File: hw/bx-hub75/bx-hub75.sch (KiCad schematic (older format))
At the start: 11 parts, among them J1 DB9_Male, U1 74HCT541, U2 74HCT541, U3 LD1117S33TR_SOT223, U4 25LCxxx, U5 SN65HVD77D

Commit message: hw/bx-hub75: oshw logo, text, extension header
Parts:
- added EXT1: EXT_HEADER, Random:EXT_HEADER, symbol Random:EXT_HEADER
- renumbered U4 to EEPROM1, U5 to RS485
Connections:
- net +3V3: now also EXT1.2 (3V3)
- net GND: now also EXT1.1 (GND)
- net MISO: now also EXT1.5 (MISO)
- net MOSI: now also EXT1.4 (MOSI)
- net SCK: now also EXT1.3 (SCK)
- net SC_EXT: now reaches FPGA1.21 (IO_20)
- net SC_EXT: now also EXT1.6 (SC)
- net EXT_IO1: now reaches FPGA1.22 (IO_21)
- net EXT_IO1: now also EXT1.7 (IO_1)
- net EXT_IO2: now reaches FPGA1.23 (IO_22)
- net EXT_IO2: now also EXT1.8 (IO_2)
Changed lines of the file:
@@
 G1
 $Comp
-L Random:SN65HVD77D U5
+L Random:SN65HVD77D RS485
 U 1 1 5BECF5D6
 P 7600 5150
-F 0 "U5" H 7600 5525 50  0000 C CNN
+F 0 "RS485" H 7600 5525 50  0000 C CNN
 F 1 "SN65HVD77D" H 7600 5434 50  0000 C CNN
 F 2 "Package_SO:SOIC-8_3.9x4.9mm_P1.27mm" H 7600 4900 50  0001 C CNN
@@
 	3400 5000 3150 5000
 $Comp
-L Memory_EEPROM:25LCxxx U4
+L Memory_EEPROM:25LCxxx EEPROM1
 U 1 1 5BF300CE
 P 5100 5100
-F 0 "U4" H 5100 5578 50  0000 C CNN
+F 0 "EEPROM1" H 5100 5578 50  0000 C CNN
 F 1 "25LCxxx" H 5100 5487 50  0000 C CNN
 F 2 "Package_SO:SOIC-8_3.9x4.9mm_P1.27mm" H 5100 5100 50  0001 C CNN
@@
 	8100 2350 8100 2250
 Connection ~ 8100 2250
+$Comp
+L Random:EXT_HEADER EXT1
+U 1 1 5BFBA84B
+P 9350 2450
+F 0 "EXT1" H 9528 2401 50  0000 L CNN
+F 1 "EXT_HEADER" H 9528 2310 50  0000 L CNN
+F 2 "Random:EXT_HEADER" H 9350 2800 50  0001 C CNN
+F 3 "" H 9350 2800 50  0001 C CNN
+	1    9350 2450
+	1    0    0    -1
+$EndComp
+$Comp
+L power:GND #PWR0116
+U 1 1 5BFBAE0E
+P 8800 2050
+F 0 "#PWR0116" H 8800 1800 50  0001 C CNN
+F 1 "GND" H 8805 1877 50  0000 C CNN
+F 2 "" H 8800 2050 50  0001 C CNN
+F 3 "" H 8800 2050 50  0001 C CNN
+	1    8800 2050
+	1    0    0    -1
+$EndComp
+$Comp
+L power:+3V3 #PWR0117
+U 1 1 5BFBAE5B
+P 8600 2300
+F 0 "#PWR0117" H 8600 2150 50  0001 C CNN
+F 1 "+3V3" H 8615 2473 50  0000 C CNN
+F 2 "" H 8600 2300 50  0001 C CNN
+F 3 "" H 8600 2300 50  0001 C CNN
+	1    8600 2300
+	1    0    0    -1
+$EndComp
+Wire Wire Line
+	8600 2300 9050 2300
+Wire Wire Line
+	9050 2200 9050 2050
+Wire Wire Line
+	9050 2050 8800 2050
+Text Label 9050 2400 2    50   ~ 0
+SCK
+Text Label 9050 2500 2    50   ~ 0
+MOSI
+Text Label 9050 2600 2    50   ~ 0
+MISO
+Text Label 9050 2700 2    50   ~ 0
+SC_EXT
+Text Label 9050 2800 2    50   ~ 0
+EXT_IO1
+Text Label 9050 2900 2    50   ~ 0
+EXT_IO2
+Text Label 2350 2750 2    50   ~ 0
+SC_EXT
+Text Label 2350 2850 2    50   ~ 0
+EXT_IO1
+Text Label 2350 2950 2    50   ~ 0
+EXT_IO2
 $EndSCHEMATC

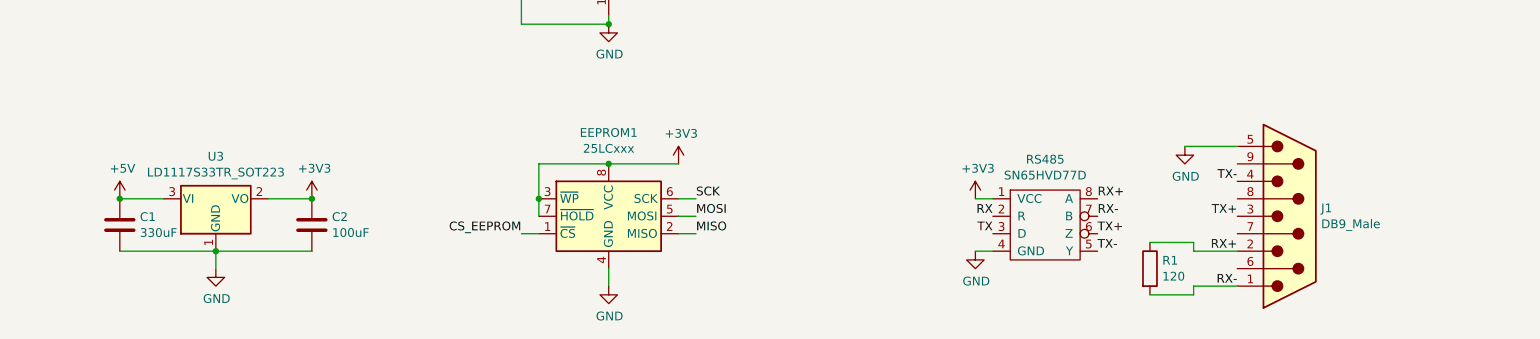
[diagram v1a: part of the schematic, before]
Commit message: hw/bx-hub75: add barrel jack
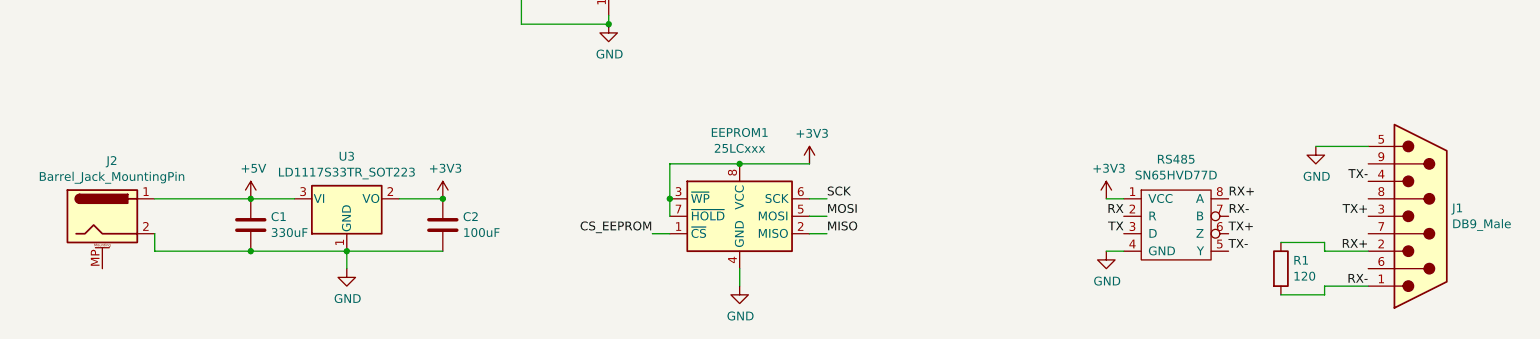
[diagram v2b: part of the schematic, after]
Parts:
- added J2: Barrel_Jack_MountingPin, Connector_BarrelJack:BarrelJack_CUI_PJ-063AH_Horizontal, symbol Connector:Barrel_Jack_MountingPin
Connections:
- net +5V: now also J2.1
- net GND: now also J2.2
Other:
- moved on the sheet: C1, C2, EEPROM1, J1, R1, RS485, U3

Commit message: hw/bx-hub75: allow bom generation with kibom
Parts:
- CHAIN1, EXT1, FPGA1: fit_field (none) -> DNF
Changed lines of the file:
@@
 F 2 "TinyFPGA:TinyFPGA_BX" H 3000 3550 50  0001 C CNN
 F 3 "" H 3000 3550 50  0001 C CNN
+F 4 "DNF" H 2850 2850 50  0001 C CNN "fit_field"
 	1    2850 2850
 	-1   0    0    1
@@
 F 2 "Random:HUB75_HEADER" H 6350 2550 50  0001 C CNN
 F 3 "" H 6350 2550 50  0001 C CNN
+F 4 "DNF" H 6350 3000 50  0001 C CNN "fit_field"
 	1    6350 3000
 	1    0    0    -1
@@
 F 2 "Random:EXT_HEADER" H 9350 2800 50  0001 C CNN
 F 3 "" H 9350 2800 50  0001 C CNN
+F 4 "DNF" H 9350 2450 50  0001 C CNN "fit_field"
 	1    9350 2450
 	1    0    0    -1

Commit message: hw/bx-hub75: V0.2 PCB/SCH.
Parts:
- added JP1: Jumper_NO_Small, Connector_PinHeader_2.54mm:PinHeader_1x02_P2.54mm_Vertical, symbol Device:Jumper_NO_Small
- added R2: 120, Resistor_SMD:R_1210_3225Metric_Pad1.42x2.65mm_HandSolder, symbol Device:R
- EXT1: footprint Random:EXT_HEADER -> Connector_PinHeader_2.54mm:PinHeader_1x08_P2.54mm_Vertical
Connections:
- net +5V: now also JP1.2
- net TX+: now also R2.2
- net TX-: now also R2.1
- net at J1.6: now also JP1.1
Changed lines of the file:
@@
 F 1 "SN65HVD77D" H 8350 5434 50  0000 C CNN
 F 2 "Package_SO:SOIC-8_3.9x4.9mm_P1.27mm" H 8350 4900 50  0001 C CNN
-F 3 "" H 8350 4900 50  0001 C CNN
+F 3 "http://www.ti.com/lit/ds/symlink/sn65hvd77.pdf" H 8350 4900 50  0001 C CNN
 	1    8350 5150
 	1    0    0    -1
@@
 L power:GND #PWR0109
 U 1 1 5BEDE34B
-P 9150 4700
-F 0 "#PWR0109" H 9150 4450 50  0001 C CNN
-F 1 "GND" H 9155 4527 50  0000 C CNN
-F 2 "" H 9150 4700 50  0001 C CNN
-F 3 "" H 9150 4700 50  0001 C CNN
-	1    9150 4700
-	1    0    0    -1
-$EndComp
-Wire Wire Line
-	9150 4700 9450 4700
+P 9150 4400
+F 0 "#PWR0109" H 9150 4150 50  0001 C CNN
+F 1 "GND" H 9155 4227 50  0000 C CNN
+F 2 "" H 9150 4400 50  0001 C CNN
+F 3 "" H 9150 4400 50  0001 C CNN
+	1    9150 4400
+	1    0    0    -1
+$EndComp
 $Comp
 L Device:R R1
@@
 F 0 "EXT1" H 9528 2401 50  0000 L CNN
 F 1 "EXT_HEADER" H 9528 2310 50  0000 L CNN
-F 2 "Random:EXT_HEADER" H 9350 2800 50  0001 C CNN
+F 2 "Connector_PinHeader_2.54mm:PinHeader_1x08_P2.54mm_Vertical" H 9350 2800 50  0001 C CNN
 F 3 "" H 9350 2800 50  0001 C CNN
 F 4 "DNF" H 9350 2450 50  0001 C CNN "fit_field"
@@
 	2500 5300 3050 5300
 Connection ~ 3050 5300
+$Comp
+L Device:R R2
+U 1 1 5C0B21F0
+P 8950 5000
+F 0 "R2" H 9020 5046 50  0000 L CNN
+F 1 "120" H 9020 4955 50  0000 L CNN
+F 2 "Resistor_SMD:R_1210_3225Metric_Pad1.42x2.65mm_HandSolder" V 8880 5000 50  0001 C CNN
+F 3 "~" H 8950 5000 50  0001 C CNN
+F 4 "dnf" H 8950 5000 50  0001 C CNN "fit_field"
+	1    8950 5000
+	1    0    0    -1
+$EndComp
+Wire Wire Line
+	8950 5150 9200 5150
+Wire Wire Line
+	9200 5150 9200 5100
+Wire Wire Line
+	9200 5100 9450 5100
+Wire Wire Line
+	9450 4900 9200 4900
+Wire Wire Line
+	9200 4900 9200 4850
+Wire Wire Line
+	9200 4850 8950 4850
+Wire Wire Line
+	9450 4700 9450 4400
+Wire Wire Line
+	9450 4400 9150 4400
+$Comp
+L power:+5V #PWR0118
+U 1 1 5C0C1F94
+P 10000 5950
+F 0 "#PWR0118" H 10000 5800 50  0001 C CNN
+F 1 "+5V" H 10015 6123 50  0000 C CNN
+F 2 "" H 10000 5950 50  0001 C CNN
+F 3 "" H 10000 5950 50  0001 C CNN
+	1    10000 5950
+	1    0    0    -1
+$EndComp
+$Comp
+L Device:Jumper_NO_Small JP1
+U 1 1 5C0C5F7A
+P 9600 5950
+F 0 "JP1" H 9600 6135 50  0000 C CNN
+F 1 "Jumper_NO_Small" H 9600 6044 50  0000 C CNN
+F 2 "Connector_PinHeader_2.54mm:PinHeader_1x02_P2.54mm_Vertical" H 9600 5950 50  0001 C CNN
+F 3 "~" H 9600 5950 50  0001 C CNN
+	1    9600 5950
+	1    0    0    -1
+$EndComp
+Wire Wire Line
+	9450 5400 9250 5400
+Wire Wire Line
+	9250 5400 9250 5950
+Wire Wire Line
+	9500 5950 9250 5950
+Wire Wire Line
+	10000 5950 9700 5950
 $EndSCHEMATC

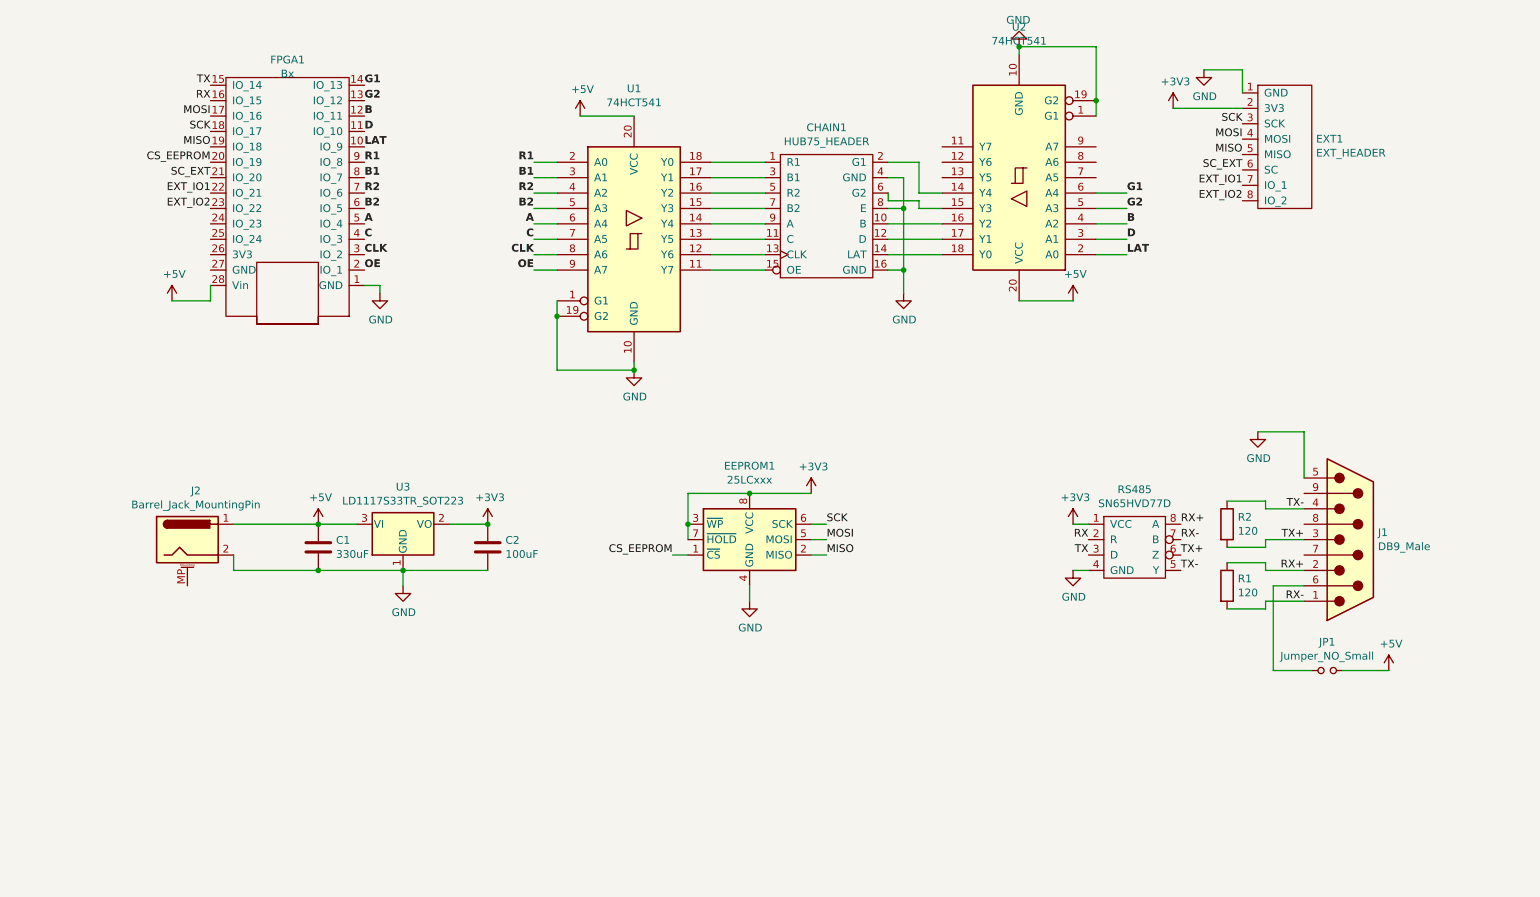
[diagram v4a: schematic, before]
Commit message: hw/bx-hub75: v0.3, E Line support.
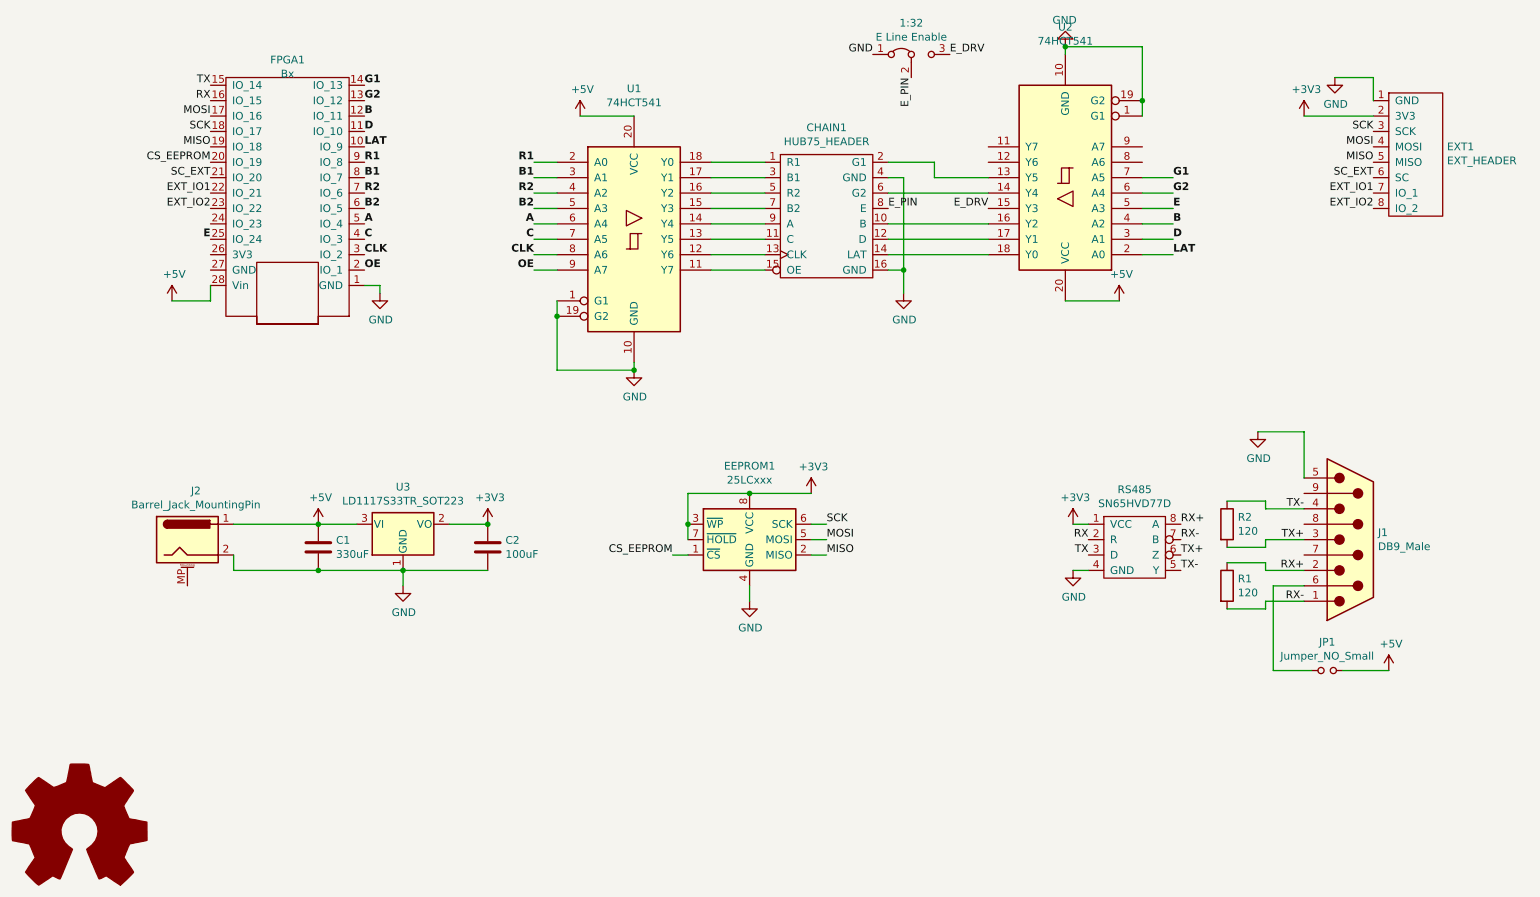
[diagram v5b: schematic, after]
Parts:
- added 1:32: E Line Enable, Connector_PinHeader_2.54mm:PinHeader_1x03_P2.54mm_Vertical, symbol Jumper:Jumper_3_Bridged12
- added OSHW1: Logo_Open_Hardware_Large, Symbol:OSHW-Logo2_9.8x8mm_SilkScreen, symbol Graphic:Logo_Open_Hardware_Large
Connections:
- net G1: now also U2.7 (A5); no longer U2.6 (A4)
- net G2: now also U2.6 (A4); no longer U2.5 (A3)
- net GND: now also 1:32.1 (A); no longer CHAIN1.8 (E)
- net E: now reaches FPGA1.25 (IO_24)
- net E: now also U2.5 (A3)
- net at CHAIN1.2 (G1): now also U2.13 (Y5); no longer U2.14 (Y4)
- net at CHAIN1.6 (G2): now also U2.14 (Y4); no longer U2.15 (Y3)
- new net E_DRV: 1:32.3 (B), U2.15 (Y3)
- new net E_PIN: 1:32.2 (C), CHAIN1.8 (E)
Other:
- moved on the sheet: EXT1, U2
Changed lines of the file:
@@
 L power:GND #PWR0103
 U 1 1 5BECC23F
-P 7600 1900
-F 0 "#PWR0103" H 7600 1650 50  0001 C CNN
-F 1 "GND" H 7605 1727 50  0000 C CNN
-F 2 "" H 7600 1900 50  0001 C CNN
-F 3 "" H 7600 1900 50  0001 C CNN
-	1    7600 1900
+P 7900 1900
+F 0 "#PWR0103" H 7900 1650 50  0001 C CNN
+F 1 "GND" H 7905 1727 50  0000 C CNN
+F 2 "" H 7900 1900 50  0001 C CNN
+F 3 "" H 7900 1900 50  0001 C CNN
+	1    7900 1900
 	-1   0    0    1
 $EndComp
 Wire Wire Line
-	7600 1950 7600 1900
+	7900 1950 7900 1900
 $Comp
 L power:GND #PWR0104
@@
 L power:+5V #PWR0107
 U 1 1 5BEDB676
-P 7950 3550
-F 0 "#PWR0107" H 7950 3400 50  0001 C CNN
-F 1 "+5V" H 7965 3723 50  0000 C CNN
-F 2 "" H 7950 3550 50  0001 C CNN
-F 3 "" H 7950 3550 50  0001 C CNN
-	1    7950 3550
-	1    0    0    -1
-$EndComp
-Wire Wire Line
-	7950 3550 7600 3550
+P 8250 3550
+F 0 "#PWR0107" H 8250 3400 50  0001 C CNN
+F 1 "+5V" H 8265 3723 50  0000 C CNN
+F 2 "" H 8250 3550 50  0001 C CNN
+F 3 "" H 8250 3550 50  0001 C CNN
+	1    8250 3550
+	1    0    0    -1
+$EndComp
+Wire Wire Line
+	8250 3550 7900 3550
 Wire Wire Line
 	5100 2350 4750 2350
 Wire Wire Line
-	8100 2250 8100 1900
-Wire Wire Line
-	8100 1900 7600 1900
-Connection ~ 7600 1900
+	8400 2250 8400 1900
+Wire Wire Line
+	8400 1900 7900 1900
+Connection ~ 7900 1900
 Text Label 4450 2650 2    50   ~ 10
 R1
@@
 	4600 3350 4450 3350
 Wire Wire Line
-	6850 3350 6850 2950
-Wire Wire Line
 	6850 2750 6750 2750
-Wire Wire Line
-	6750 2950 6850 2950
-Connection ~ 6850 2950
-Wire Wire Line
-	6850 2950 6850 2750
-Wire Wire Line
-	7100 3250 6750 3250
-Wire Wire Line
-	7100 3150 6750 3150
-Wire Wire Line
-	7100 3050 6750 3050
-Wire Wire Line
-	7100 2950 6950 2950
-Wire Wire Line
-	6950 2950 6950 2900
-Wire Wire Line
-	6950 2900 6750 2900
-Wire Wire Line
-	6750 2900 6750 2850
-Wire Wire Line
-	7100 2850 6950 2850
-Wire Wire Line
-	6950 2650 6750 2650
-Wire Wire Line
-	6950 2650 6950 2850
-Text Label 8300 3250 0    50   ~ 10
+Text Label 8600 3250 0    50   ~ 10
 LAT
-Text Label 8300 3150 0    50   ~ 10
+Text Label 8600 3150 0    50   ~ 10
 D
-Text Label 8300 3050 0    50   ~ 10
+Text Label 8600 3050 0    50   ~ 10
 B
-Text Label 8300 2950 0    50   ~ 10
+Text Label 8600 2850 0    50   ~ 10
 G2
-Text Label 8300 2850 0    50   ~ 10
+Text Label 8600 2750 0    50   ~ 10
 G1
 Wire Wire Line
-	8300 3250 8100 3250
-Wire Wire Line
-	8300 3150 8100 3150
-Wire Wire Line
-	8300 3050 8100 3050
-Wire Wire Line
-	8300 2950 8100 2950
-Wire Wire Line
-	8300 2850 8100 2850
+	8600 3250 8400 3250
+Wire Wire Line
+	8600 3150 8400 3150
+Wire Wire Line
+	8600 3050 8400 3050
+Wire Wire Line
+	8600 2850 8400 2850
+Wire Wire Line
+	8600 2750 8400 2750
 Wire Wire Line
 	6850 3350 6850 3500
@@
 L 74xx:74HCT541 U2
 U 1 1 5BF6300B
-P 7600 2750
-F 0 "U2" H 7600 1772 50  0000 C CNN
-F 1 "74HCT541" H 7600 1863 50  0000 C CNN
-F 2 "Package_SO:SOIC-20W_7.5x12.8mm_P1.27mm" H 7600 2750 50  0001 C CNN
-F 3 "http://www.ti.com/lit/gpn/sn74HCT541" H 7600 2750 50  0001 C CNN
-	1    7600 2750
+P 7900 2750
+F 0 "U2" H 7900 1772 50  0000 C CNN
+F 1 "74HCT541" H 7900 1863 50  0000 C CNN
+F 2 "Package_SO:SOIC-20W_7.5x12.8mm_P1.27mm" H 7900 2750 50  0001 C CNN
+F 3 "http://www.ti.com/lit/gpn/sn74HCT541" H 7900 2750 50  0001 C CNN
+	1    7900 2750
 	-1   0    0    1
 $EndComp
 Wire Wire Line
-	8100 2350 8100 2250
-Connection ~ 8100 2250
+	8400 2350 8400 2250
+Connection ~ 8400 2250
 $Comp
 L Random:EXT_HEADER EXT1
 U 1 1 5BFBA84B
-P 9350 2450
-F 0 "EXT1" H 9528 2401 50  0000 L CNN
-F 1 "EXT_HEADER" H 9528 2310 50  0000 L CNN
-F 2 "Connector_PinHeader_2.54mm:PinHeader_1x08_P2.54mm_Vertical" H 9350 2800 50  0001 C CNN
-F 3 "" H 9350 2800 50  0001 C CNN
-F 4 "DNF" H 9350 2450 50  0001 C CNN "fit_field"
-	1    9350 2450
+P 10200 2500
+F 0 "EXT1" H 10378 2451 50  0000 L CNN
+F 1 "EXT_HEADER" H 10378 2360 50  0000 L CNN
+F 2 "Connector_PinHeader_2.54mm:PinHeader_1x08_P2.54mm_Vertical" H 10200 2850 50  0001 C CNN
+F 3 "" H 10200 2850 50  0001 C CNN
+F 4 "DNF" H 10200 2500 50  0001 C CNN "fit_field"
+	1    10200 2500
 	1    0    0    -1
 $EndComp
@@
 L power:GND #PWR0116
 U 1 1 5BFBAE0E
-P 8800 2050
-F 0 "#PWR0116" H 8800 1800 50  0001 C CNN
-F 1 "GND" H 8805 1877 50  0000 C CNN
-F 2 "" H 8800 2050 50  0001 C CNN
-F 3 "" H 8800 2050 50  0001 C CNN
-	1    8800 2050
+P 9650 2100
+F 0 "#PWR0116" H 9650 1850 50  0001 C CNN
+F 1 "GND" H 9655 1927 50  0000 C CNN
+F 2 "" H 9650 2100 50  0001 C CNN
+F 3 "" H 9650 2100 50  0001 C CNN
+	1    9650 2100
 	1    0    0    -1
 $EndComp
@@
 L power:+3V3 #PWR0117
 U 1 1 5BFBAE5B
-P 8600 2300
-F 0 "#PWR0117" H 8600 2150 50  0001 C CNN
-F 1 "+3V3" H 8615 2473 50  0000 C CNN
-F 2 "" H 8600 2300 50  0001 C CNN
-F 3 "" H 8600 2300 50  0001 C CNN
-	1    8600 2300
-	1    0    0    -1
-$EndComp
-Wire Wire Line
-	8600 2300 9050 2300
-Wire Wire Line
-	9050 2200 9050 2050
-Wire Wire Line
-	9050 2050 8800 2050
-Text Label 9050 2400 2    50   ~ 0
+P 9450 2350
+F 0 "#PWR0117" H 9450 2200 50  0001 C CNN
+F 1 "+3V3" H 9465 2523 50  0000 C CNN
+F 2 "" H 9450 2350 50  0001 C CNN
+F 3 "" H 9450 2350 50  0001 C CNN
+	1    9450 2350
+	1    0    0    -1
+$EndComp
+Wire Wire Line
+	9450 2350 9900 2350
+Wire Wire Line
+	9900 2250 9900 2100
+Wire Wire Line
+	9900 2100 9650 2100
+Text Label 9900 2450 2    50   ~ 0
 SCK
-Text Label 9050 2500 2    50   ~ 0
+Text Label 9900 2550 2    50   ~ 0
 MOSI
-Text Label 9050 2600 2    50   ~ 0
+Text Label 9900 2650 2    50   ~ 0
 MISO
-Text Label 9050 2700 2    50   ~ 0
+Text Label 9900 2750 2    50   ~ 0
 SC_EXT
-Text Label 9050 2800 2    50   ~ 0
+Text Label 9900 2850 2    50   ~ 0
 EXT_IO1
-Text Label 9050 2900 2    50   ~ 0
+Text Label 9900 2950 2    50   ~ 0
 EXT_IO2
 Text Label 2350 2750 2    50   ~ 0
@@
 Wire Wire Line
 	10000 5950 9700 5950
+Wire Wire Line
+	6850 2750 6850 3350
+Text Label 6750 2950 0    50   ~ 0
+E_PIN
+Wire Wire Line
+	6750 3250 7400 3250
+Wire Wire Line
+	6750 3050 7400 3050
+Wire Wire Line
+	7400 3150 6750 3150
+Text Label 7400 2950 2    50   ~ 0
+E_DRV
+Text Label 8600 2950 0    50   ~ 10
+E
+Wire Wire Line
+	8600 2950 8400 2950
+Wire Wire Line
+	6750 2850 7400 2850
+Wire Wire Line
+	6750 2650 7050 2650
+Wire Wire Line
+	7050 2650 7050 2750
+Wire Wire Line
+	7050 2750 7400 2750
+$Comp
+L Jumper:Jumper_3_Bridged12 1:32
+U 1 1 5C2221F2
+P 6900 1950
+F 0 "1:32" H 6900 2154 50  0000 C CNN
+F 1 "E Line Enable" H 6900 2063 50  0000 C CNN
+F 2 "Connector_PinHeader_2.54mm:PinHeader_1x03_P2.54mm_Vertical" H 6900 1950 50  0001 C CNN
+F 3 "~" H 6900 1950 50  0001 C CNN
+	1    6900 1950
+	1    0    0    -1
+$EndComp
+Text Label 6900 2100 3    50   ~ 0
+E_PIN
+Text Label 6650 1950 2    50   ~ 0
+GND
+Text Label 7150 1950 0    50   ~ 0
+E_DRV
+Text Label 2350 3150 2    50   ~ 10
+E
+$Comp
+L Graphic:Logo_Open_Hardware_Large OSHW1
+U 1 1 5C225D36
+P 1500 7000
+F 0 "OSHW1" H 1500 7500 50  0001 C CNN
+F 1 "Logo_Open_Hardware_Large" H 1500 6600 50  0001 C CNN
+F 2 "Symbol:OSHW-Logo2_9.8x8mm_SilkScreen" H 1500 7000 50  0001 C CNN
+F 3 "~" H 1500 7000 50  0001 C CNN
+	1    1500 7000
+	1    0    0    -1
+$EndComp
 $EndSCHEMATC
